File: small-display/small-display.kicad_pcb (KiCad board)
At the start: 2 copper layers, 43 x 63 mm, 27 parts, among them J1 USB_C_Receptacle_USB2.0, J2 Micro_SD_Card_Det, J3 Conn_01x40, J5 F32D-1A7Y1-21040, U1 TPD4EUSB30, U2 74LVC1G07SE-7, U3 RT9742GGJ5, U4 PAM2804AAB010, U5 USB2412-DZK, Y1 ECS-240-8-33-AGN-TR

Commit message: Minor changes.
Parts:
- removed J3: Conn_01x40, Connector_PinSocket_2.54mm:PinSocket_2x20_P2.54mm_Vertical
- added U6: NLVVHC1G04DFT1G, airball-hardware:SOT65P210X110-5N, F.Cu at (35.8, 46.5)
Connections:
- net /PWM renamed GPIO_02_PWM
- J5 pad 11: /DAT_CMD -> GPIO_26_DAT_CMD
- J5 pad 12: /!WRITE -> GPIO_07_!WRITE
- J5 pad 14: /DB0 -> GPIO_08_DB0
- J5 pad 15: /DB1 -> GPIO_09_DB1
- J5 pad 16: /DB2 -> GPIO_10_DB2
- J5 pad 17: /DB3 -> GPIO_11_DB3
- J5 pad 18: /DB4 -> GPIO_12_DB4
- J5 pad 19: /DB5 -> GPIO_13_DB5
- J5 pad 20: /DB6 -> GPIO_14_DB6
- J5 pad 21: /DB7 -> GPIO_15_DB7
- J5 pad 22: /DB8 -> GPIO_16_DB8
- J5 pad 23: /DB9 -> GPIO_17_DB9
- J5 pad 24: /DB10 -> GPIO_18_DB10
- J5 pad 25: /DB11 -> GPIO_19_DB11
- J5 pad 26: /DB12 -> GPIO_20_DB12
- J5 pad 27: /DB13 -> GPIO_21_DB13
- J5 pad 28: /DB14 -> GPIO_22_DB14
- J5 pad 29: /DB15 -> GPIO_23_DB15
- J5 pad 30: /!RESET -> GPIO_27_!RESET
- U1 pad 4: Net-(U1-Pad4) -> unconnected-(U1-Pad4)
- U1 pad 5: Net-(U1-Pad5) -> unconnected-(U1-Pad5)
- U1 pad 6: Net-(U1-Pad5) -> unconnected-(U1-Pad5)
- U1 pad 7: Net-(U1-Pad4) -> unconnected-(U1-Pad4)
- U5 pad 13: unconnected-(U5-Pad13) -> GND
- U5 pad 17: unconnected-(U5-Pad17) -> Net-(U5-Pad17)
- U5 pad 18: unconnected-(U5-Pad18) -> +3.3V
- U5 pad 19: unconnected-(U5-Pad19) -> GND
- U5 pad 25: unconnected-(U5-Pad25) -> Net-(U5-Pad25)
- U5 pad 26: unconnected-(U5-Pad26) -> Net-(U5-Pad26)
- U5 pad 9: unconnected-(U5-Pad9) -> Net-(U5-Pad9)

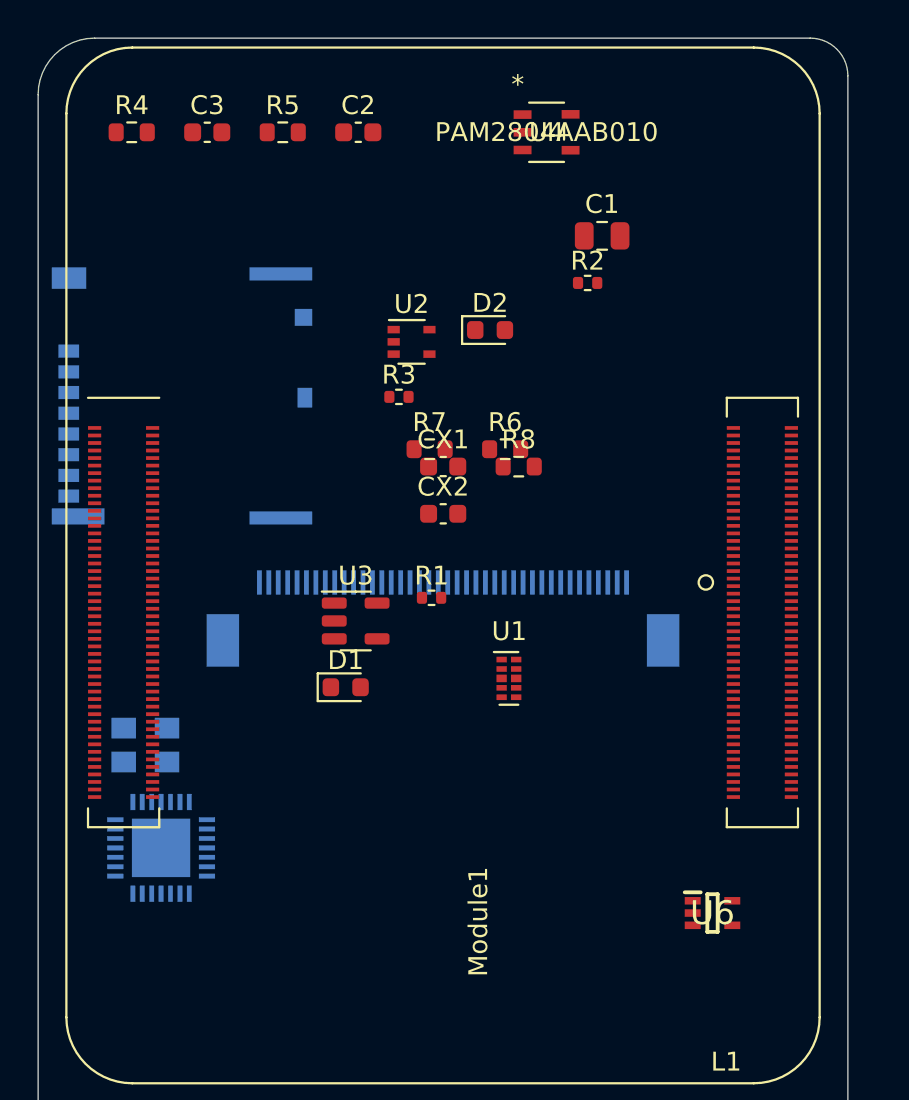
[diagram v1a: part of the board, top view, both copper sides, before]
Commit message: Continued work on small display PCB.
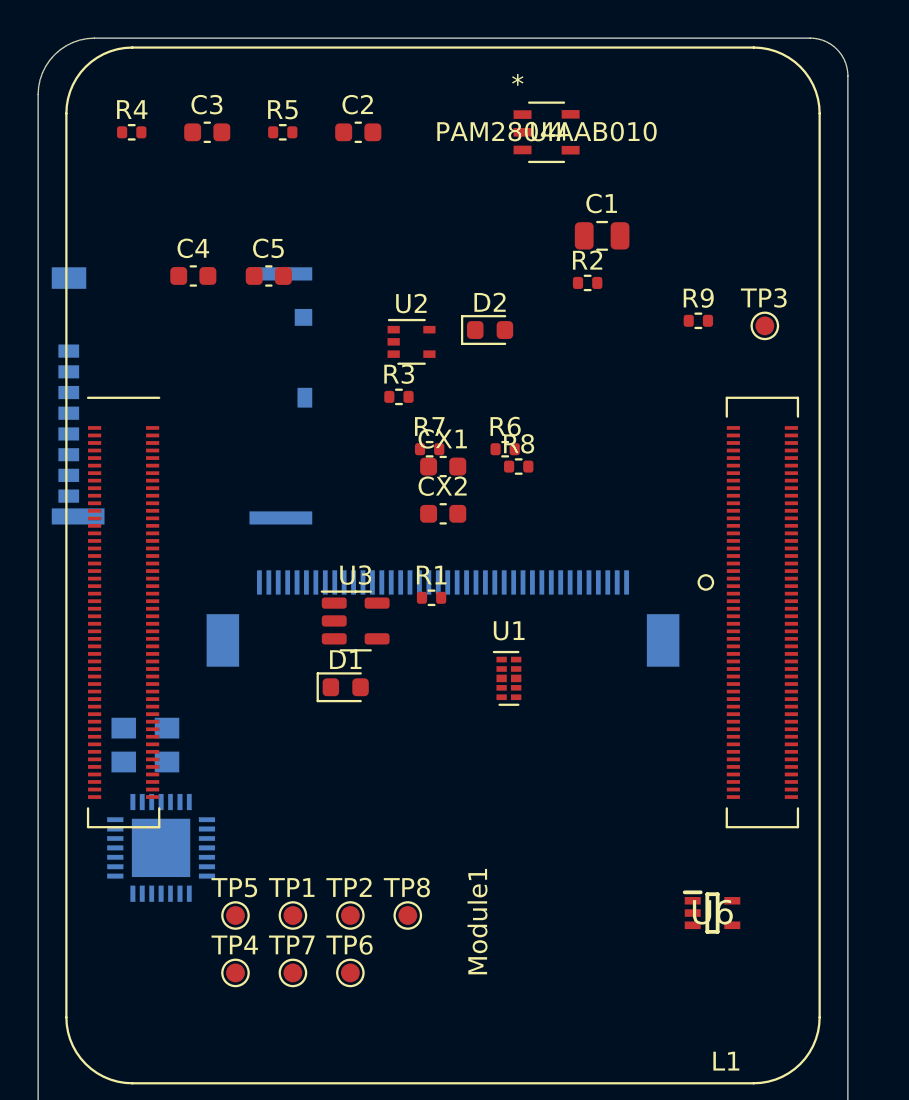
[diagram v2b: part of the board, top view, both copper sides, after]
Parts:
- added C4: 0.1 uF, Capacitor_SMD:C_0603_1608Metric, F.Cu at (8.24, 12.6)
- added C5: 0.1 uF, Capacitor_SMD:C_0603_1608Metric, F.Cu at (12.2, 12.6)
- added R9: 12k 1%, Resistor_SMD:R_0402_1005Metric, F.Cu at (35.1, 15.0)
- added TP1: TestPoint, TestPoint:TestPoint_Pad_D1.0mm, F.Cu at (13.5, 46.6)
- added TP2: TestPoint, TestPoint:TestPoint_Pad_D1.0mm, F.Cu at (16.6, 46.6)
- added TP3: TestPoint, TestPoint:TestPoint_Pad_D1.0mm, F.Cu at (38.6, 15.3)
- added TP4: TestPoint, TestPoint:TestPoint_Pad_D1.0mm, F.Cu at (10.5, 49.6)
- added TP5: TestPoint, TestPoint:TestPoint_Pad_D1.0mm, F.Cu at (10.5, 46.6)
- added TP6: TestPoint, TestPoint:TestPoint_Pad_D1.0mm, F.Cu at (16.6, 49.6)
- added TP7: TestPoint, TestPoint:TestPoint_Pad_D1.0mm, F.Cu at (13.5, 49.6)
- added TP8: TestPoint, TestPoint:TestPoint_Pad_D1.0mm, F.Cu at (19.6, 46.6)
- R4, R5, R6, R7, R8: footprint Resistor_SMD:R_0603_1608Metric -> Resistor_SMD:R_0402_1005Metric
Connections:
- net GPIO_02_PWM renamed GPIO_25_PWM
- U6 pad 2: USB_RESET -> GPIO_02_USB_!RESET

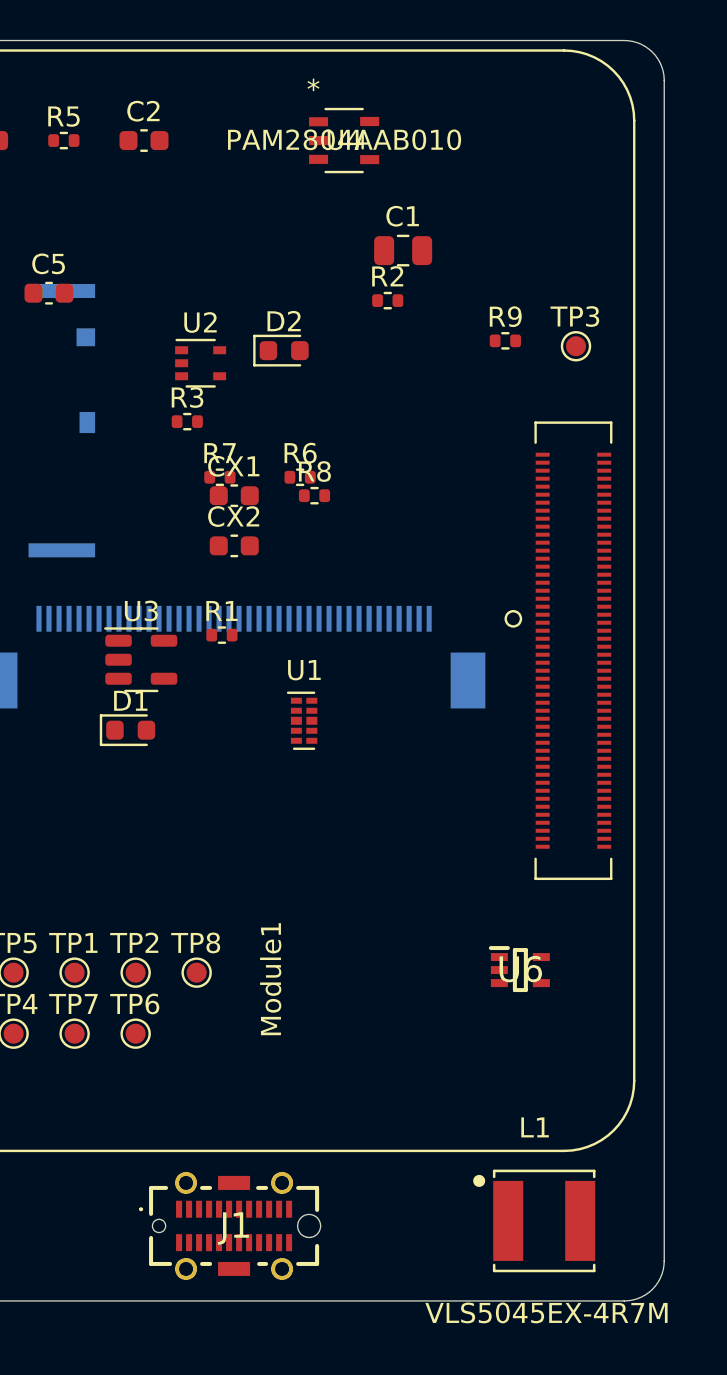
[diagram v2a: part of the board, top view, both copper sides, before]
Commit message: More work on small display.
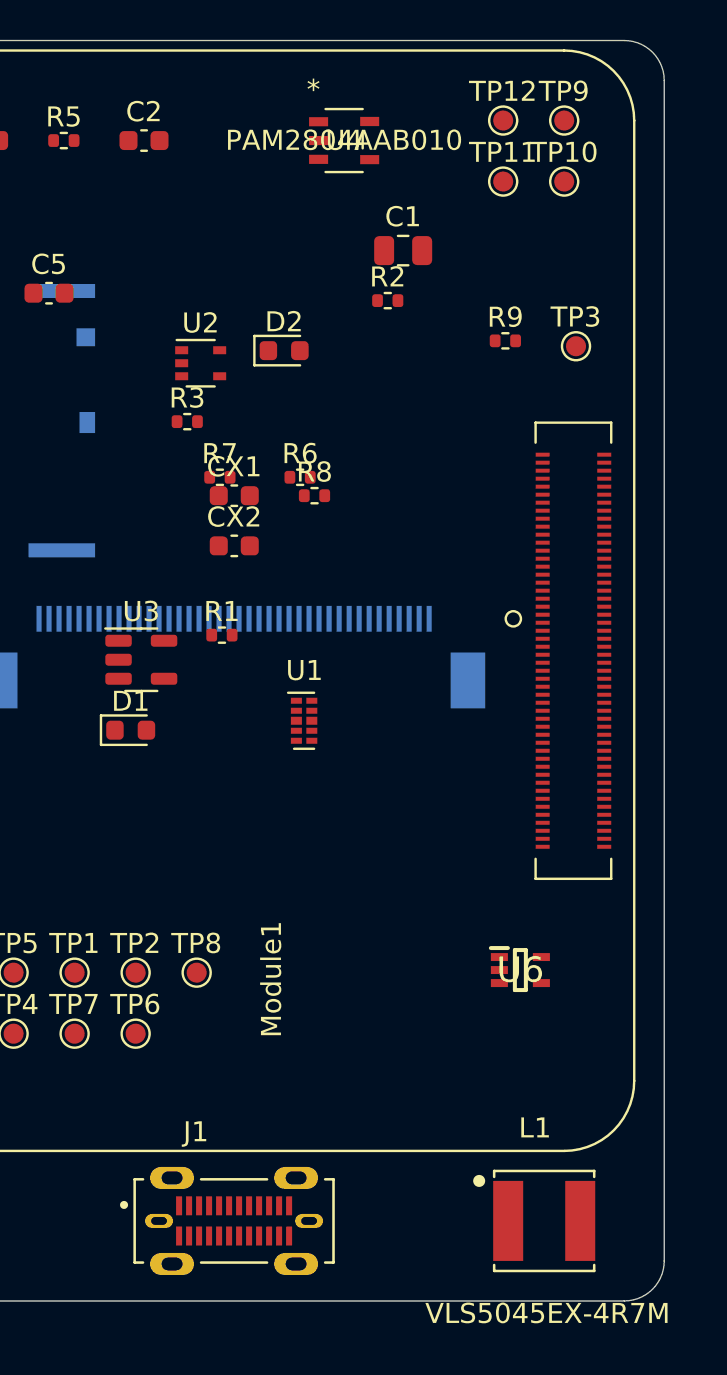
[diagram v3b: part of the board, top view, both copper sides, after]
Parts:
- added TP10: TestPoint, TestPoint:TestPoint_Pad_D1.0mm, F.Cu at (38.0, 7.05)
- added TP11: TestPoint, TestPoint:TestPoint_Pad_D1.0mm, F.Cu at (35.0, 7.05)
- added TP12: TestPoint, TestPoint:TestPoint_Pad_D1.0mm, F.Cu at (35.0, 4.00)
- added TP9: TestPoint, TestPoint:TestPoint_Pad_D1.0mm, F.Cu at (38.0, 4.00)
- J1: value USB_C_Receptacle_USB2.0 -> 2047110001; footprint CM4IO:USB411503C -> airball-hardware:MOLEX_2047110001
- moved J1 0.25 mm to (21.5, 59.0)
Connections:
- J1 pad A10: (no net) -> unconnected-(J1-PadA10)
- J1 pad A11: (no net) -> unconnected-(J1-PadA11)
- J1 pad A2: (no net) -> unconnected-(J1-PadA2)
- J1 pad A3: (no net) -> unconnected-(J1-PadA3)
- J1 pad B10: (no net) -> unconnected-(J1-PadB10)
- J1 pad B11: (no net) -> unconnected-(J1-PadB11)
- J1 pad B2: (no net) -> unconnected-(J1-PadB2)
- J1 pad B3: (no net) -> unconnected-(J1-PadB3)

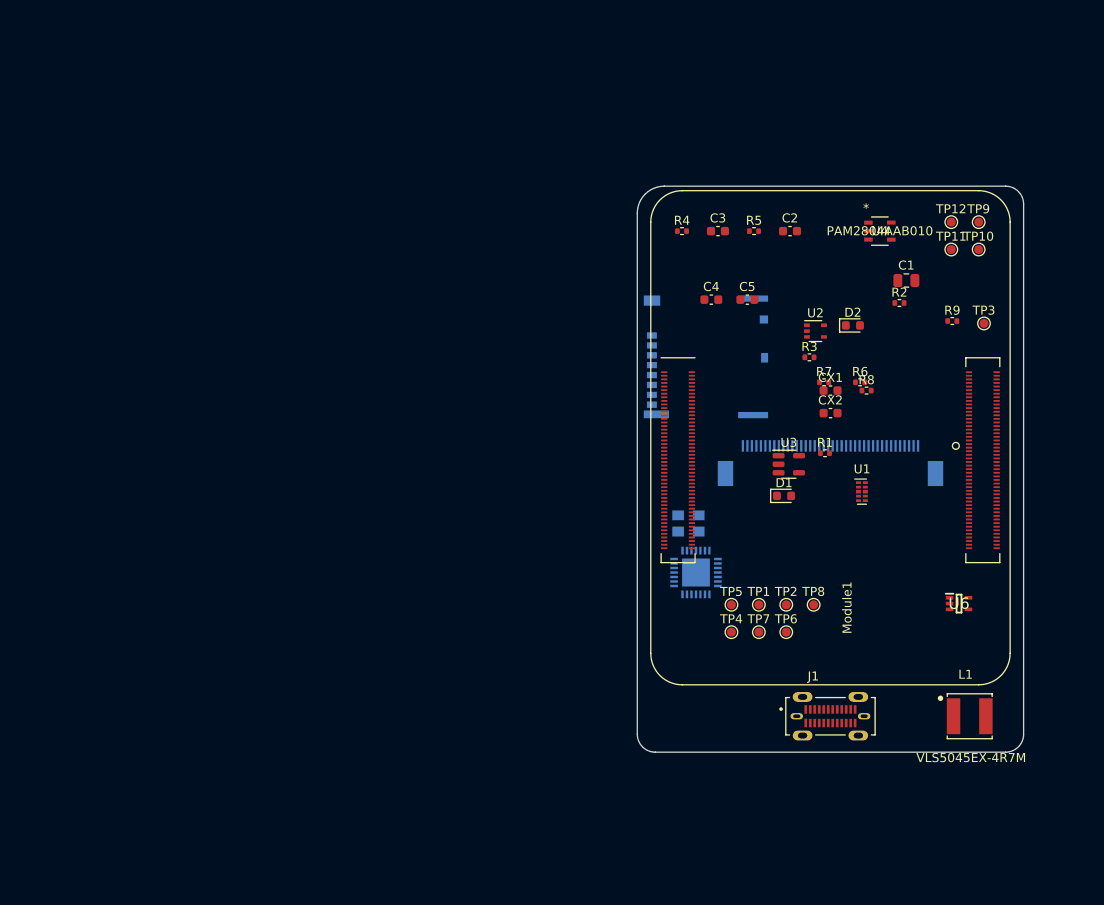
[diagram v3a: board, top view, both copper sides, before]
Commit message: More routing and design of small display.
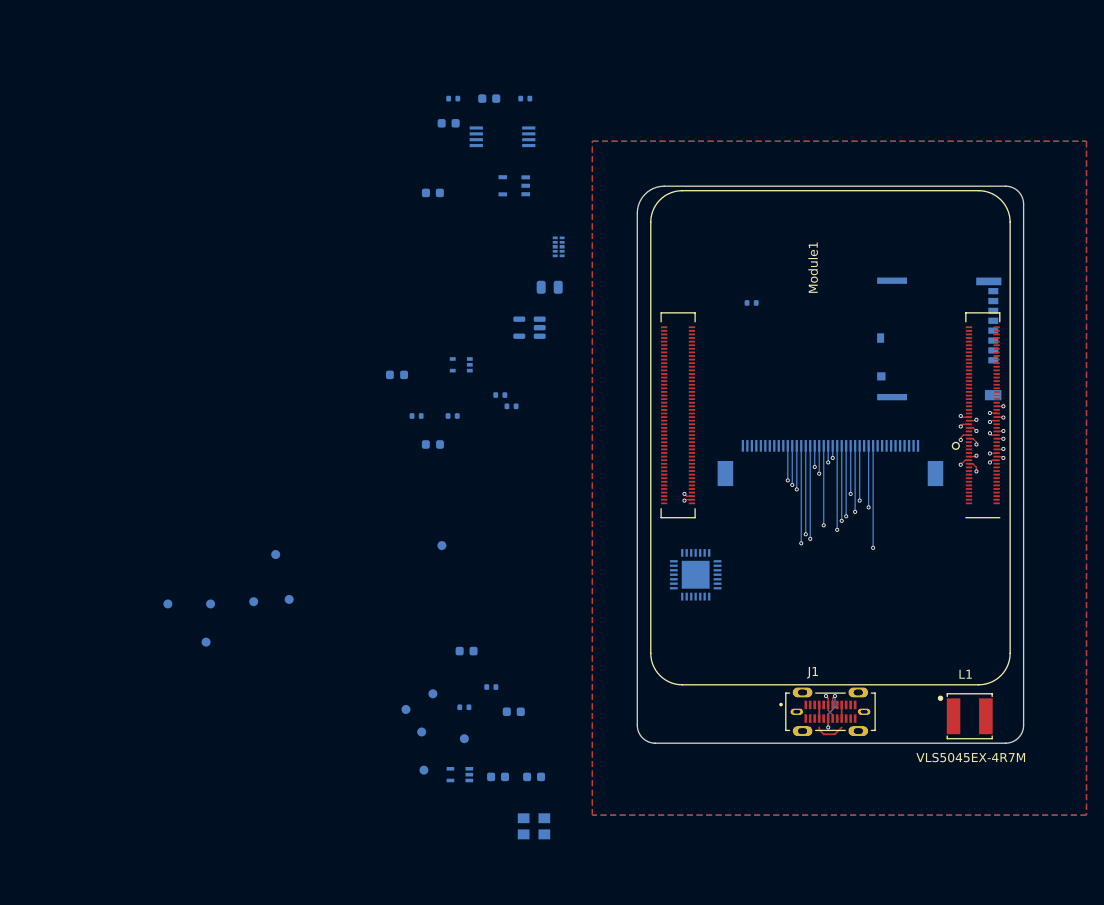
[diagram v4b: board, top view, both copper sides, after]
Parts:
- removed the TP10 at (38.0, 7.05)
- added C6: 0.1uF, Capacitor_SMD:C_0603_1608Metric, B.Cu at (-21.0, -7.00)
- added TP11: TestPoint, TestPoint:TestPoint_Pad_D1.0mm, B.Cu at (-22.8, 56.5)
- added U7: M24M01-DFDW6TP, airball-hardware:TSSOP_FDW6TP_STM, B.Cu at (-15.0, -5.50)
- C1, C2, C3, C4, C5, CX1, CX2, D1, D2, R1, R2, R3, R4, R5, R6, R7, R8, R9, TP1, TP12, TP2, TP3, TP4, TP5, TP6, TP7, TP8, TP9, U1, U2, U3, U4, U6: moved to B.Cu
- TP10: renamed from TP11; moved to B.Cu
- moved TP3 93.6 mm to (-48.0, 50.8), turned to 180 degrees
- moved TP9 83.7 mm to (-25.8, 58.2), turned to 180 degrees
- moved TP12 79.0 mm to (-19.2, 61.5), turned to 180 degrees
- moved R9 69.3 mm to (-19.2, 58.0), turned to 180 degrees
- moved TP7 65.9 mm to (-52.2, 46.5), turned to 180 degrees
- moved TP10 65.6 mm to (-21.8, 40.0), turned to 180 degrees
- moved TP2 64.1 mm to (-47.5, 46.5), turned to 180 degrees
- moved TP8 60.1 mm to (-40.2, 41.0), turned to 180 degrees
- moved C5 59.9 mm to (-15.5, 65.8), turned to 180 degrees
- moved U6 58.7 mm to (-19.8, 65.5), turned to 180 degrees
- moved Module1 58.2 mm to (38.0, 4.00), turned to 180 degrees
- moved C4 56.7 mm to (-11.5, 65.8), turned to 180 degrees
- moved TP1 56.2 mm to (-42.7, 46.2), turned to 180 degrees
- moved R8 53.2 mm to (-16.2, 55.8), turned to 180 degrees
- moved D2 51.0 mm to (-26.8, 21.0), turned to 180 degrees
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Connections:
- net /+1.8v renamed +1.8v
- net /+3.3v renamed GPIO_VREF
- net /AIN0 renamed AIN0
- net /AIN1 renamed AIN1
- net /ETH_LEDG renamed ETH_LEDG
- net /ETH_LEDY renamed ETH_LEDY
- net /GPIO24 renamed GPIO24
- net /GPIO3 renamed GPIO3
- net /GPIO4 renamed GPIO4
- net /GPIO5 renamed GPIO5
- net /GPIO6 renamed GPIO6
- net /ID_SC renamed ID_SC
- net /ID_SD renamed ID_SD
- net /RUN_PG renamed RUN_PG
- net /SD_CLK renamed SD_CLK
- net /SD_CMD renamed SD_CMD
- net /SD_DAT0 renamed SD_DAT0
- net /SD_DAT1 renamed SD_DAT1
- net /SD_DAT2 renamed SD_DAT2
- net /SD_DAT3 renamed SD_DAT3
- net /SD_PWR_ON renamed SD_PWR_ON
- net /TRD0_P renamed TRD0_P
- net /TRD2_N renamed TRD2_N
- net /TRD2_P renamed TRD2_P
- net /TRD3_N renamed TRD3_N
- net /TRD3_P renamed TRD3_P
- net /USBOTG_ID renamed USBOTG_ID
- net /nEXTRST renamed nEXTRST
- C1 pad 2: GND -> TRD1_N
- C2 pad 2: GND -> TRD1_N
- C3 pad 2: GND -> TRD1_N
- C4 pad 2: GND -> TRD1_N
- C5 pad 2: GND -> TRD1_N
- CX1 pad 2: GND -> TRD1_N
- CX2 pad 2: GND -> TRD1_N
- J1 pad A1: GND -> TRD1_N
- J1 pad A12: GND -> TRD1_N
- J1 pad B1: GND -> TRD1_N
- J1 pad B12: GND -> TRD1_N
- J1 pad S1: GND -> TRD1_N
- J1 pad S2: GND -> TRD1_N
- J1 pad S3: GND -> TRD1_N
- J1 pad S4: GND -> TRD1_N
- J1 pad S5: GND -> TRD1_N
- J1 pad S6: GND -> TRD1_N
- J2 pad 11: GND -> TRD1_N
- J2 pad 6: GND -> TRD1_N
- J5 pad 1: GND -> TRD1_N
- J5 pad 10: GND -> TRD1_N
- J5 pad 13: +3V3 -> +3.3V
- J5 pad 31: GND -> TRD1_N
- J5 pad 33: GND -> TRD1_N
- J5 pad 39: GND -> TRD1_N
- J5 pad 7: +3V3 -> +3.3V
- J5 pad 8: +3V3 -> +3.3V
- Module1 pad 1: GND -> TRD1_N
- Module1 pad 10: /TRD0_N -> TRD1_N
- Module1 pad 107: GND -> TRD1_N
- Module1 pad 108: GND -> TRD1_N
- Module1 pad 113: GND -> TRD1_N
- Module1 pad 114: GND -> TRD1_N
- Module1 pad 119: GND -> TRD1_N
- Module1 pad 120: GND -> TRD1_N
- Module1 pad 125: GND -> TRD1_N
- Module1 pad 126: GND -> TRD1_N
- Module1 pad 13: GND -> TRD1_N
- Module1 pad 131: GND -> TRD1_N
- Module1 pad 132: GND -> TRD1_N
- Module1 pad 137: GND -> TRD1_N
- Module1 pad 138: GND -> TRD1_N
- Module1 pad 14: GND -> TRD1_N
- Module1 pad 144: GND -> TRD1_N
- Module1 pad 150: GND -> TRD1_N
- Module1 pad 155: GND -> TRD1_N
- Module1 pad 156: GND -> TRD1_N
- Module1 pad 16: /SYNC_IN -> TRD1_N
- Module1 pad 161: GND -> TRD1_N
- Module1 pad 162: GND -> TRD1_N
- Module1 pad 167: GND -> TRD1_N
- Module1 pad 168: GND -> TRD1_N
- Module1 pad 173: GND -> TRD1_N
- Module1 pad 174: GND -> TRD1_N
- Module1 pad 179: GND -> TRD1_N
- Module1 pad 18: /SYNC_OUT -> TRD1_N
- Module1 pad 180: GND -> TRD1_N
- Module1 pad 185: GND -> TRD1_N
- Module1 pad 186: GND -> TRD1_N
- Module1 pad 191: GND -> TRD1_N
- Module1 pad 192: GND -> TRD1_N
- Module1 pad 197: GND -> TRD1_N
- Module1 pad 198: GND -> TRD1_N
- Module1 pad 2: GND -> TRD1_N
- Module1 pad 20: /EEPROM_nWP -> TRD1_N
- Module1 pad 22: GND -> TRD1_N
- Module1 pad 23: GND -> TRD1_N
- Module1 pad 24: /GPIO26 -> GPIO_26_DAT_CMD
- Module1 pad 25: /GPIO21 -> GPIO_21_DB13
- Module1 pad 26: /GPIO19 -> GPIO_19_DB11
- Module1 pad 27: /GPIO20 -> GPIO_20_DB12
- Module1 pad 28: /GPIO13 -> GPIO_13_DB5
- Module1 pad 29: /GPIO16 -> GPIO_16_DB8
- Module1 pad 31: /GPIO12 -> GPIO_12_DB4
- Module1 pad 32: GND -> TRD1_N
- Module1 pad 33: GND -> TRD1_N
- Module1 pad 37: /GPIO7 -> GPIO_07_!WRITE
- Module1 pad 38: /GPIO11 -> GPIO_11_DB3
- Module1 pad 39: /GPIO8 -> GPIO_08_DB0
- Module1 pad 4: /TRD1_P -> TRD1_N
- Module1 pad 40: /GPIO9 -> GPIO_09_DB1
- Module1 pad 41: /GPIO25 -> GPIO_25_PWM
- Module1 pad 42: GND -> TRD1_N
- Module1 pad 43: GND -> TRD1_N
- Module1 pad 44: /GPIO10 -> GPIO_10_DB2
- Module1 pad 46: /GPIO22 -> GPIO_22_DB14
- Module1 pad 47: /GPIO23 -> GPIO_23_DB15
- Module1 pad 48: /GPIO27 -> GPIO_27_!RESET
- Module1 pad 49: /GPIO18 -> GPIO_18_DB10
- Module1 pad 50: /GPIO17 -> GPIO_17_DB9
- Module1 pad 51: /GPIO15 -> GPIO_15_DB7
- Module1 pad 52: GND -> TRD1_N
- Module1 pad 53: GND -> TRD1_N
- Module1 pad 55: /GPIO14 -> GPIO_14_DB6
- Module1 pad 58: /GPIO2 -> GPIO_02_USB_!RESET
- Module1 pad 59: GND -> TRD1_N
- Module1 pad 6: /TRD1_N -> TRD1_N
- Module1 pad 60: GND -> TRD1_N
- Module1 pad 65: GND -> TRD1_N
- Module1 pad 66: GND -> TRD1_N
- Module1 pad 7: GND -> TRD1_N
- Module1 pad 71: GND -> TRD1_N
- Module1 pad 74: GND -> TRD1_N
- Module1 pad 76: /Reserved -> unconnected-(Module1-Pad76)
- Module1 pad 77: /+5v -> +5V
- Module1 pad 79: /+5v -> +5V
- Module1 pad 8: GND -> TRD1_N
- Module1 pad 80: /SCL0 -> SCL0
- Module1 pad 81: /+5v -> +5V
- Module1 pad 82: /SDA0 -> SDA0
- Module1 pad 83: /+5v -> +5V
- Module1 pad 85: /+5v -> +5V
- Module1 pad 87: /+5v -> +5V
- Module1 pad 97: /CAM_GPIO -> unconnected-(Module1-Pad97)
- Module1 pad 98: GND -> TRD1_N
- R4 pad 2: GND -> TRD1_N
- R5 pad 2: GND -> TRD1_N
- R6 pad 1: GND -> TRD1_N
- R7 pad 1: GND -> TRD1_N
- R9 pad 2: GND -> TRD1_N
- TP12 pad 1: USBD_N -> USBD_P
- U1 pad 3: GND -> TRD1_N
- U1 pad 8: GND -> TRD1_N
- U2 pad 3: GND -> TRD1_N
- U3 pad 2: GND -> TRD1_N
- U4 pad 2: GND -> TRD1_N
- U5 pad 13: GND -> TRD1_N
- U5 pad 15: GND -> TRD1_N
- U5 pad 19: GND -> TRD1_N
- U5 pad 29: GND -> TRD1_N
- U6 pad 3: GND -> TRD1_N
- Y1 pad 2: GND -> TRD1_N
- Y1 pad 4: GND -> TRD1_N
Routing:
- net GPIO_21_DB13: track 0.00 -> 36.4 mm, vias 0 -> 2
- net GPIO_20_DB12: track 0.00 -> 36.2 mm, vias 0 -> 2
- net GPIO_19_DB11: track 0.00 -> 31.6 mm, vias 0 -> 2
- net GPIO_16_DB8: track 0.00 -> 31.6 mm, vias 0 -> 2
- net GPIO_12_DB4: track 0.00 -> 30.6 mm, vias 0 -> 2
- net GPIO_23_DB15: track 0.00 -> 30.2 mm, vias 0 -> 2
- net GPIO_13_DB5: track 0.00 -> 29.1 mm, vias 0 -> 2
- net GPIO_27_!RESET: track 0.00 -> 28.5 mm, vias 0 -> 2
- net GPIO_26_DAT_CMD: track 0.00 -> 27.8 mm, vias 0 -> 2
- net GPIO_22_DB14: track 0.00 -> 27.2 mm, vias 0 -> 2
- net GPIO_11_DB3: track 0.00 -> 26.9 mm, vias 0 -> 2
- net GPIO_18_DB10: track 0.00 -> 26.9 mm, vias 0 -> 2
- net GPIO_07_!WRITE: track 0.00 -> 26.0 mm, vias 0 -> 2
- net GPIO_08_DB0: track 0.00 -> 24.7 mm, vias 0 -> 2
- net GPIO_14_DB6: track 0.00 -> 23.5 mm, vias 0 -> 2
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- added copper zone on In1.Cu, net +3.3V
- added copper zone on In2.Cu, net +5V
- added copper zone on B.Cu, net TRD1_N
- added copper zone on F.Cu, net TRD1_N
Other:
- board size 43 x 63 mm -> 43 x 62 mm
- copper layers 2 -> 4
